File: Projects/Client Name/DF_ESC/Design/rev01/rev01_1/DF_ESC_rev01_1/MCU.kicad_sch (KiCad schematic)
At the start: 0 parts

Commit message: Update 14-01-2023
Block diagram
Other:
- title: Title of the project -> DF_ESC_rev01_1
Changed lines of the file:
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@@
   (paper "A4")
   (title_block
-    (title "Title of the project")
+    (title "DF_ESC_rev01_1")
     (date "2024-01-14")
-    (rev "rev01")
+    (rev "rev01_1")
     (company "Ivan Mendez IMA Design")
     (comment 3 "i.mendezalon@hotmail.com")
     (comment 4 "Ivan Mendez")
   )
-  (sheet_instances
-    (path "/" (page "1"))
-  )
 )

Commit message: Update MCU.kicad_sch
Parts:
- added U1: STM32F405RGTx, Package_QFP:LQFP-64_10x10mm_P0.5mm, symbol MCU_ST_STM32F4:STM32F405RGTx
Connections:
- new net: U1.18 (VSS), U1.63 (VSS)
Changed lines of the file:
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@@
     (comment 4 "Ivan Mendez")
   )
+  (symbol (lib_id "MCU_ST_STM32F4:STM32F405RGTx") (at 160.02 96.52 0) (unit 1)
+    (in_bom yes) (on_board yes) (dnp no) (fields_autoplaced)
+    (property "Reference" "U1" (at 164.7541 142.24 0)
+      (effects (font (size 1.27 1.27)) (justify left))
+    )
+    (property "Value" "STM32F405RGTx" (at 164.7541 144.78 0)
+      (effects (font (size 1.27 1.27)) (justify left))
+    )
+    (property "Footprint" "Package_QFP:LQFP-64_10x10mm_P0.5mm" (at 144.78 139.7 0)
+      (effects (font (size 1.27 1.27)) (justify right) hide)
+    )
+    (property "Datasheet" "https://www.st.com/resource/en/datasheet/stm32f405rg.pdf" (at 160.02 96.52 0)
+      (effects (font (size 1.27 1.27)) hide)
+    )
+    (pin "19")
+    (pin "24")
+    (pin "37")
+    (pin "12")
+    (pin "4")
+    (pin "49")
+    (pin "59")
+    (pin "61")
+    (pin "62")
+    (pin "43")
+    (pin "63")
+    (pin "64")
+    (pin "7")
+    (pin "8")
+    (pin "9")
+    (pin "50")
+    (pin "16")
+    (pin "20")
+    (pin "33")
+    (pin "48")
+    (pin "5")
+    (pin "51")
+    (pin "44")
+    (pin "28")
+    (pin "52")
+    (pin "30")
+    (pin "17")
+    (pin "34")
+    (pin "54")
+    (pin "15")
+    (pin "42")
+    (pin "39")
+    (pin "41")
+    (pin "3")
+    (pin "40")
+    (pin "1")
+    (pin "56")
+    (pin "22")
+    (pin "35")
+    (pin "10")
+    (pin "36")
+    (pin "13")
+    (pin "47")
+    (pin "53")
+    (pin "57")
+    (pin "58")
+    (pin "27")
+    (pin "55")
+    (pin "6")
+    (pin "60")
+    (pin "25")
+    (pin "32")
+    (pin "38")
+    (pin "11")
+    (pin "26")
+    (pin "21")
+    (pin "31")
+    (pin "45")
+    (pin "2")
+    (pin "46")
+    (pin "18")
+    (pin "29")
+    (pin "14")
+    (pin "23")
+    (instances
+      (project "DF_ESC_rev01_1"
+        (path "/e63e39d7-6ac0-4ffd-8aa3-1841a4541b55/138932fe-f685-46a1-bb06-1768136a532b"
+          (reference "U1") (unit 1)
+        )
+      )
+    )
+  )
 )

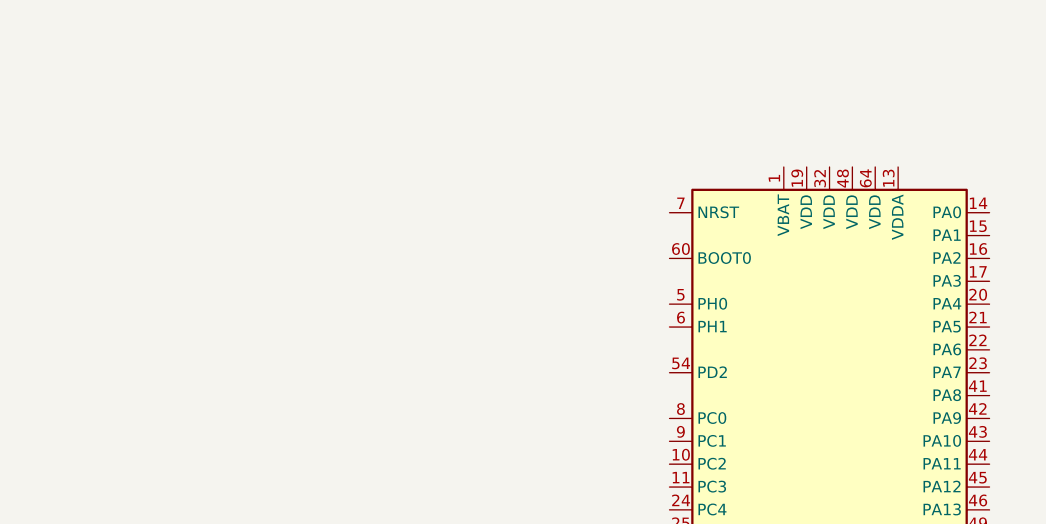
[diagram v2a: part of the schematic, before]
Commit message: Update 18-01-2024
MCU - Decoupling capacitor zone
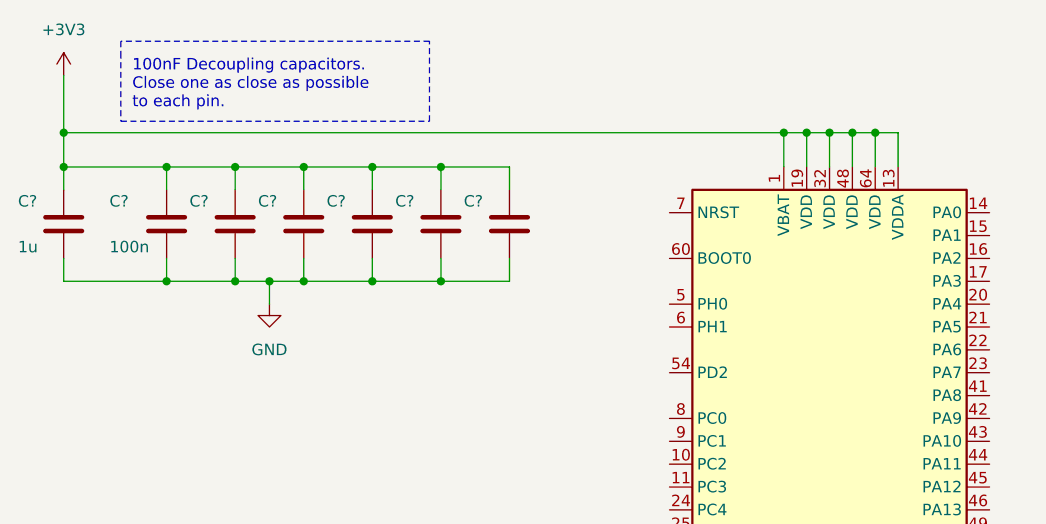
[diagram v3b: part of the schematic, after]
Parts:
- added C? (x6): 100n, symbol Device:C
- added C?: 1u, symbol Device:C
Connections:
- net +3V3: now reaches U1.1 (VBAT)
- net +3V3: now also U1.13 (VDDA), U1.19 (VDD), U1.32 (VDD), U1.48 (VDD), U1.64 (VDD), C?.1, C?.1, C?.1, C?.1, C?.1, C?.1, C?.1
- new net GND: C?.2, C?.2, C?.2, C?.2, C?.2, C?.2, C?.2
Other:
- note added: "100nF Decoupling capacitors. Close one as close as possible to each pin."

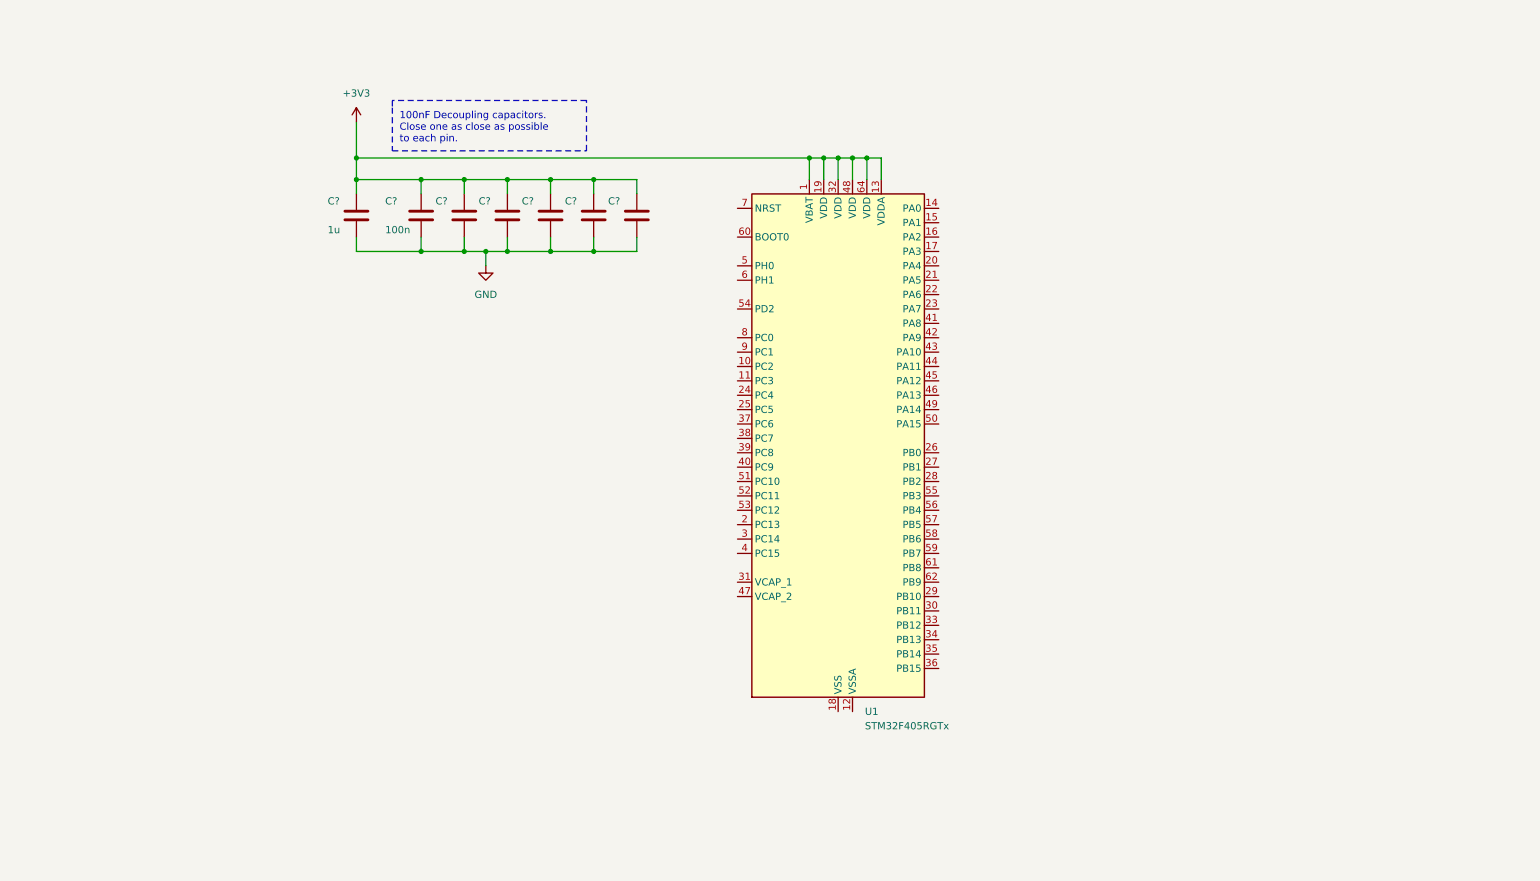
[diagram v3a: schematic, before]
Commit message: Update 19-01-2024 primera
cambiar y añadir numeracion de sheets
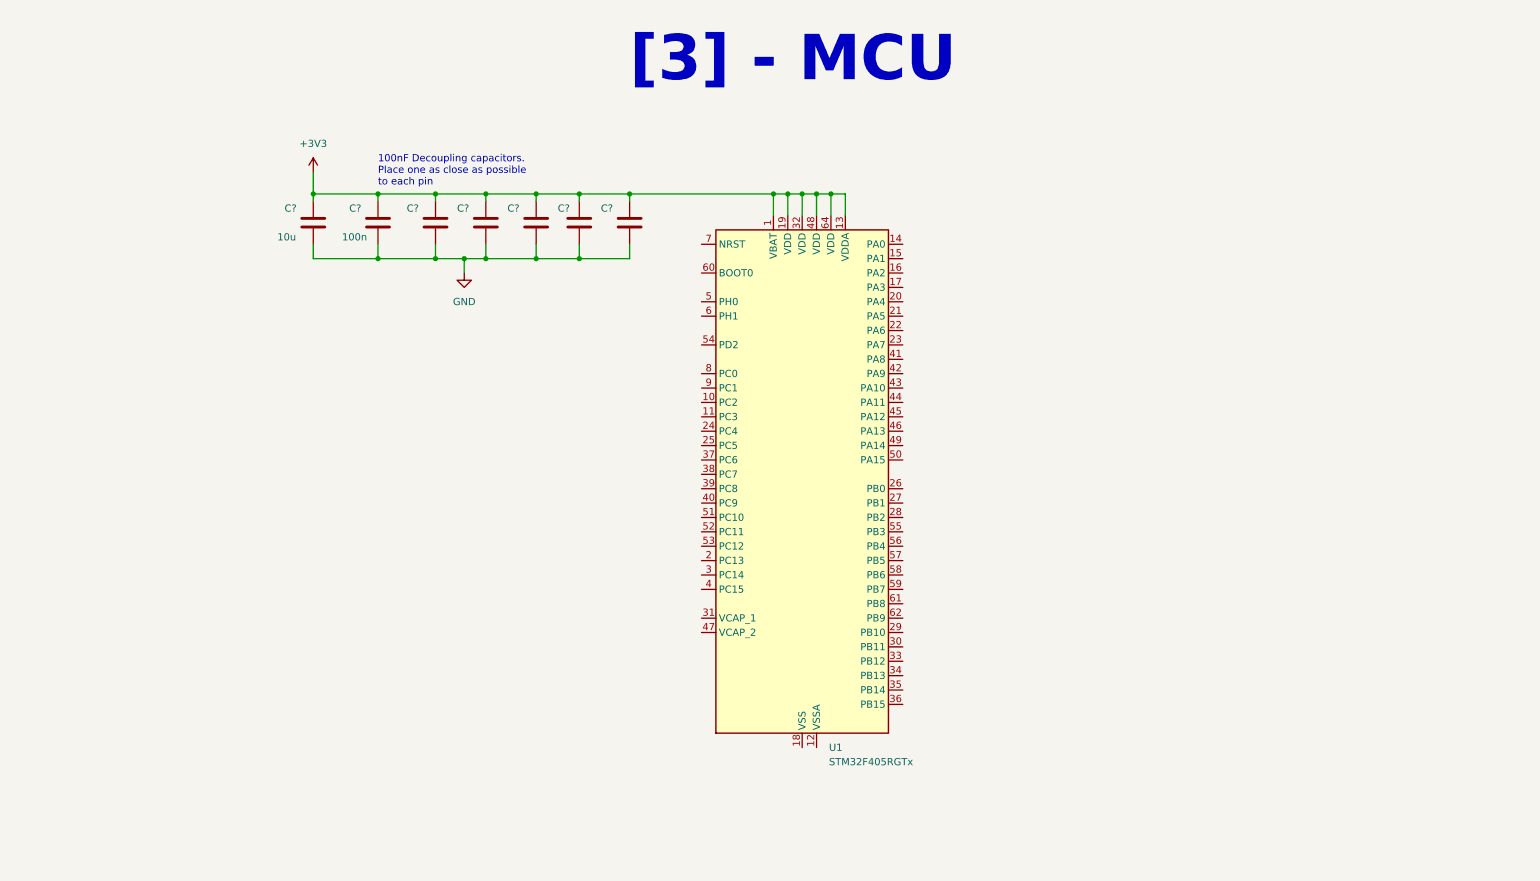
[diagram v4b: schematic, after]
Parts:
- removed C? (x6): 100n, symbol Device:C
- removed C?: 1u, symbol Device:C
- added C? (x6): 100n, symbol Device:C
- added C?: 10u, symbol Device:C
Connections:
- net +3V3: now also C?.1, C?.1, C?.1, C?.1, C?.1, C?.1, C?.1
- net GND: now also C?.2, C?.2, C?.2, C?.2, C?.2, C?.2, C?.2
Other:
- note added: "100nF Decoupling capacitors. Place one as close as possible to each pin"
- note added: "[3] - MCU"
- note removed: "100nF Decoupling capacitors. Close one as close as possible to each pin."

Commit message: Update 19-01-2024_2
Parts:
- added C?: 100n, symbol Device:C
- added R?: 0R, symbol Device:R
- added SW?: SW_DIP_x01, symbol Switch:SW_DIP_x01
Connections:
- net +3V3: now also R?.1
- net GND: now also U1.12 (VSSA), U1.18 (VSS), U1.63 (VSS), C?.2, SW?.1
- net at U1.60 (BOOT0): now also R?.2
- net NRST: now reaches U1.7 (NRST)
- net NRST: now also C?.1, SW?.2
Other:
- note added: "Set Boot mode Table 7"
- moved on the sheet: C?, U1

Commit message: Update 19-01-2024_3
MCU schematic complete
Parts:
- added C1, C? (x3): 100n, symbol Device:C
- added C? (x2): 2u2, symbol Device:C
- added C?: 1u, symbol Device:C
- added C? (x2): C, symbol Device:C
- added D?: LED_G, symbol Device:LED
- added D?: LED_R, symbol Device:LED
- added D?: LED, symbol Device:LED
- added FB?: FerriteBead, symbol Device:FerriteBead
- added J?: Conn_01x03_Pin, symbol Connector:Conn_01x03_Pin
- added J?: Conn_01x08_Pin, symbol Connector:Conn_01x08_Pin
- added J?: Conn_01x06_Pin, symbol Connector:Conn_01x06_Pin
- added R1, R2, R?: 1k, symbol Device:R
- added R3, R? (x2): 2k2, symbol Device:R
- added R?: 39k, symbol Device:R
- added R? (x2): R, symbol Device:R
- added TH?: 10k, symbol Device:Thermistor_NTC
- added Y?: Crystal_Small, symbol Device:Crystal_Small
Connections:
- net +3V3: now also C1.2, FB?.2, J?.1 (Pin_1), J?.2 (Pin_2), R?.1, TH?.1; no longer U1.13 (VDDA)
- net GND: now also C1.1, C?.1, C?.1, C?.2, C?.2, C?.2, C?.2, C?.2, C?.2, D?.1 (K), D?.1 (K), D?.1 (K), J?.2 (Pin_2), J?.3 (Pin_3), J?.3 (Pin_3), J?.8 (Pin_8), R3.1, R?.2
- net BOOT0_P: now reaches R?.2, U1.60 (BOOT0)
- net AN_IN: now reaches U1.10 (PC2)
- net AN_IN: now also C?.1, R?.1, R?.2
- net SENS3: now reaches U1.14 (PA0)
- net SENS2: now reaches U1.15 (PA1)
- net SENS1: now reaches U1.16 (PA2)
- net ADC_TEMP: now reaches U1.17 (PA3)
- net ADC_TEMP: now also R3.2, TH?.2
- net LED_GREEN: now reaches U1.24 (PC4)
- net LED_GREEN: now also R1.1
- net LED_RED: now reaches U1.25 (PC5)
- net LED_RED: now also R2.1
- net BR_S02: now reaches U1.26 (PB0)
- net BR_S01: now reaches U1.27 (PB1)
- net RX_SCL_MOSI: now reaches U1.29 (PB10)
- net RX_SCL_MOSI: now also U1.38 (PC7), J?.6 (Pin_6)
- net TX_SDA_NSS: now reaches U1.30 (PB11)
- net TX_SDA_NSS: now also U1.37 (PC6), J?.5 (Pin_5)
- net VCAP_1: now reaches U1.31 (VCAP_1)
- net VCAP_1: now also C?.1
- net DC_CAL: now reaches U1.33 (PB12)
- net L3: now reaches U1.34 (PB13)
- net L2: now reaches U1.35 (PB14)
- net L1: now reaches U1.36 (PB15)
- net H2: now reaches U1.42 (PA9)
- net H1: now reaches U1.43 (PA10)
- net USB_DM: now reaches U1.44 (PA11)
- net USB_DP: now reaches U1.45 (PA12)
- net SWDIO: now reaches U1.46 (PA13)
- net VCAP_2: now reaches U1.47 (VCAP_2)
- net VCAP_2: now also C?.1
- net SWCLK: now reaches U1.49 (PA14)
- net SWCLK: now also J?.2 (Pin_2), J?.4 (Pin_4), J?.5 (Pin_5)
- net PH_0_P: now reaches U1.5 (PH0)
- net PH_0_P: now also R?.2
- net EN_GATE: now reaches U1.51 (PC10)
- net HALL_3: now reaches U1.52 (PC11)
- net FAULT: now reaches U1.53 (PC12)
- net SERVO: now reaches U1.57 (PB5)
- net SERVO: now also C?.1, R?.1
- net HALL_1: now reaches U1.58 (PB6)
- net HALL_2: now reaches U1.59 (PB7)
- net PH_1_P: now reaches U1.6 (PH1)
- net PH_1_P: now also R?.2
- net CAN_RX: now reaches U1.61 (PB8)
- net CAN_TX: now reaches U1.62 (PB9)
- net TEMP_MOTOR: now reaches U1.8 (PC0)
- new net: J?.3 (Pin_3), R?.2
- new net: C?.1, C?.1, FB?.1, U1.13 (VDDA)
- new net: D?.2 (A), R?.2
- new net: D?.2 (A), R2.2
- new net: D?.2 (A), R1.2
- new net +5V: J?.1 (Pin_1), J?.1 (Pin_1)
- new net +VDC: R?.1
- new net MISO_ADC_EXT2: J?.7 (Pin_7)
- new net PH_0: C?.2, R?.1, Y?.2
- new net PH_1: C?.2, R?.1, Y?.1
- new net SCK_ADC_EXT: J?.4 (Pin_4)
- no-connect marks 0 -> 18
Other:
- note added: "COMMUNICATION"
- note added: "NRST internally pulled-up"
- note added: "NTC THERMISTOR"
- note added: "PROG/DEBUG"
- note added: "SERVO"
- note added: "Subtitute with 100R If used as servo output"
- note added: "VOLTAGE_DIVIDER"
- note added: "WHEN: VDC = 60V => AN_IN = 3V204"
- moved on the sheet: R?

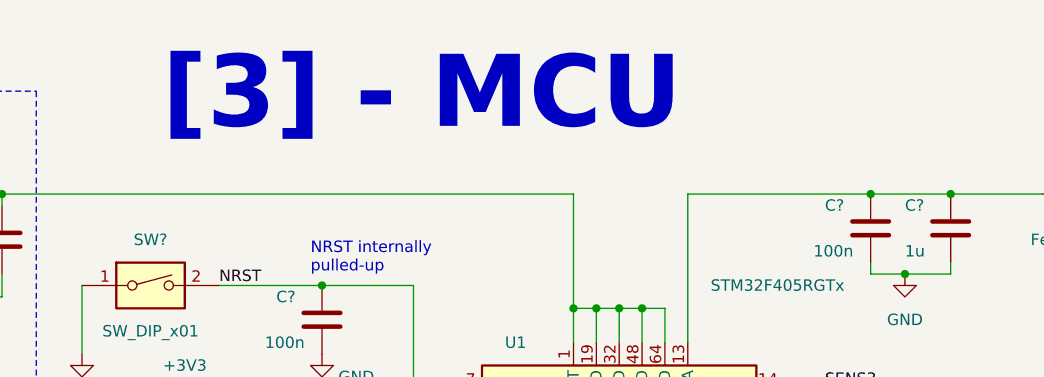
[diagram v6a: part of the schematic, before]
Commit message: Update 23-01-2024_prueba 5
Quitar la U de MCU para probar
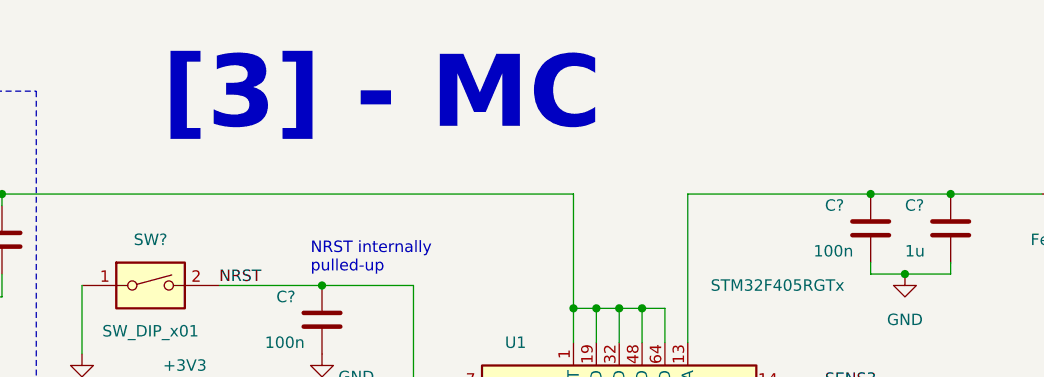
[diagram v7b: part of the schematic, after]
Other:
- note added: "[3] - MC"
- note removed: "[3] - MCU"
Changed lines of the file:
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@@
     )
   )
-  (text "[3] - MCU" (at 123.19 31.75 0)
+  (text "[3] - MC" (at 123.19 31.75 0)
     (effects (font (size 8 8) (thickness 1.6) bold) (justify left bottom))
   )

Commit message: Update MCU.kicad_sch
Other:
- note added: "[3] - MCU"
- note removed: "[3] - MC"
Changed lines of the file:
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@@
     )
   )
-  (text "[3] - MC" (at 123.19 31.75 0)
+  (text "[3] - MCU" (at 123.19 31.75 0)
     (effects (font (size 8 8) (thickness 1.6) bold) (justify left bottom))
   )
